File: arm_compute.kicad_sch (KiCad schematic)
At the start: 0 parts

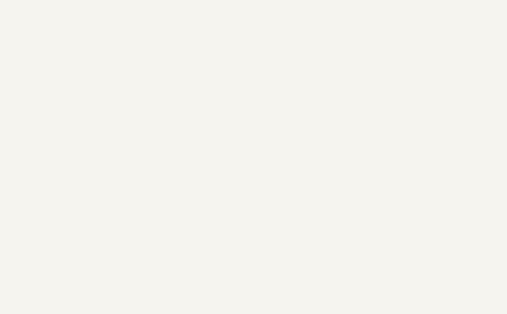
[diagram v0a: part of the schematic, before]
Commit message: add CPU_REFCLK_IN
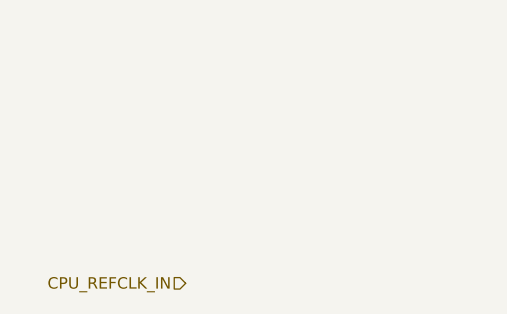
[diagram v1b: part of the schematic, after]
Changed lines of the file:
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@@
+		)
+	)
+	(hierarchical_label "CPU_REFCLK_IN"
+		(shape input)
+		(at 29.21 177.8 180)
+		(effects
+			(font
+				(size 1.27 1.27)
+			)
+			(justify right)
 		)
 	)
